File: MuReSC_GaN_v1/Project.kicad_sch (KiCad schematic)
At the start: 19 parts, among them IC1 STM32G474RET6, IC10 UCC12040DVE, IC2 TPSM5601R5HRDAR, IC3 ISO7720FQDQ1, IC4 ISO7720FQDQ1, IC5 ISO7720FQDQ1, IC6 ISO7720FQDQ1, IC7 UCC12040DVE, IC8 UCC12040DVE, IC9 UCC12040DVE, J1 62000211121, J2 62000211121, J3 691214110002, J4 691214110002, J5 691214110002, J6 691214110002

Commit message: finito schema
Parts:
- removed J1: 62000211121, 62000211121, symbol SamacSys_Parts:62000211121
- removed J3, J4, J5, J6: 691214110002, 691214110002, symbol SamacSys_Parts:691214110002
- added BEAD1, BEAD2: BLM15AG601SZ1D, NFZ15SG152SN10B, symbol SamacSys_Parts:BLM15AG601SZ1D
- added C1: C1812C124J1GACTU, C1812, symbol SamacSys_Parts:C1812C124J1GACTU
- added C2: C1206C821J1GACTU, C1206, symbol SamacSys_Parts:C1206C821J1GACTU
- added C3: C1812C105K1RACTU, C1812, symbol SamacSys_Parts:C1812C105K1RACTU
- added CCV1, CCV2: C1210C107M8PACTU, C1210, symbol SamacSys_Parts:C1210C107M8PACTU
- added CD1, CD2, CD3, CD4, CISOP1, CISOP2, CISOP3, CISOP4, CISOS1, CISOS2, CISOS3, CISOS4, CLD2, CM5, CM8: GRT155R70J105KE01D, CAPC1005X55N, symbol SamacSys_Parts:GRT155R70J105KE01D
- added CFT1, CFT2, CFT3, CFT4: NFM15PC104R1A3D, NFM15CC222D1A3D, symbol SamacSys_Parts:NFM15PC104R1A3D
- added CIN1, CIN2: GRJ31CZ72A475KE01L, CAPC3216X190N, symbol SamacSys_Parts:GRJ31CZ72A475KE01L
- added CLD1: GRM155Z71A105KE01J, CAPC1005X55N, symbol SamacSys_Parts:GRM155Z71A105KE01J
- added CM0: GRM155R61A475MEAAD, CAPC1005X55N, symbol SamacSys_Parts:GRM155R61A475MEAAD
- added CM1, CM10, CM2, CM3, CM4, CM6, CM7, CM9, CTP1, CTP2, CTP3, CTP4, CTS1, CTS2, CTS3, CTS4: C0402C104K8RAC7867, CAPC1005X55N, symbol SamacSys_Parts:C0402C104K8RAC7867
- added COH1, COH2: GJM0335C1E6R8DB01D, CAPC0603X33N, symbol SamacSys_Parts:GJM0335C1E6R8DB01D
- added COL1, COL2: C, Capacitor_SMD:C_0201_0603Metric_Pad0.64x0.40mm_HandSolder, symbol Device:C
- added CTPB1, CTPB2, CTPB3, CTPB4, CTSB1, CTSB2, CTSB3, CTSB4: C0603C106M8PAC7411, C0603, symbol SamacSys_Parts:C0603C106M8PAC7411
- added D1, D2: ESDALC6V1-1U2, ESDALC6V11U2, symbol SamacSys_Parts:ESDALC6V1-1U2
- added IC11, IC12, IC13, IC14: LMG1020YFFR, BGA6C40P2X3_86X126X62, symbol SamacSys_Parts:LMG1020YFFR
- added J1: 62000211121_x6, SamacSys_Parts:62000211121_x6, symbol SamacSys_Parts:62000211121_x6
- added J3, J4: 62000211121_x1, SamacSys_Parts:62000211121_x1, symbol SamacSys_Parts:62000211121_x1
- added L1: L, Inductor_SMD:L_0603_1608Metric, symbol Device:L
- added P1, P2: 691214110002, 691214110002, symbol SamacSys_Parts:691214110002
- added Q1, Q2, Q3, Q4: GS61004B-TR, GS61004BTR, symbol SamacSys_Parts:GS61004B-TR
- added RF1, RM1: MCS04020D1002BE000, RESC1005X37N, symbol SamacSys_Parts:MCS04020D1002BE000
- added RF2: MCS04020D2491BE000, RESC1005X37N, symbol SamacSys_Parts:MCS04020D2491BE000
- added RH1, RH2, RH3, RH4, RL1, RL2, RL3, RL4: MCS0402MC1008FE000, RESC1005X37N, symbol SamacSys_Parts:MCS0402MC1008FE000
- added RS1, RS2, RS3, RS4, RS5, RS6, RS7, RS8: R, Resistor_SMD:R_0603_1608Metric_Pad0.98x0.95mm_HandSolder, symbol Device:R
- added RUB1: MCS04020C3300FE000, RESC1005X37N, symbol SamacSys_Parts:MCS04020C3300FE000
- added RUB2: MCS04020C1003FE000, RESC1005X37N, symbol SamacSys_Parts:MCS04020C1003FE000
- added S1, S2: PTS526_SK15_SMTR2_LFS, PTS526SK15SMTR2LFS, symbol SamacSys_Parts:PTS526_SK15_SMTR2_LFS
- added Y1: NX3215SA-32.768K-STD-MUS-2, NX3215SA32768KSTDMUS2, symbol SamacSys_Parts:NX3215SA-32.768K-STD-MUS-2
- added Y2: NX3225SA-24.000MHZ-STD-CSR-1, NX3225SA24000MHZSTDCSR1, symbol SamacSys_Parts:NX3225SA-24.000MHZ-STD-CSR-1
- added Z3, Z4: TSZU52C3V3_RGG, TSZU52C3V3RGG, symbol SamacSys_Parts:TSZU52C3V3_RGG
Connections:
- net VDD3V3: now reaches IC6.1 (VCC1)
- net VDD3V3: now also IC1.1 (VBAT), IC1.16 (VDD_1), IC1.32 (VDD_2), IC1.48 (VDD_3), IC1.64 (VDD_4), IC3.1 (VCC1), IC4.1 (VCC1), IC5.1 (VCC1), PS1.4 (VOUT), BEAD2.1, CISOP1.1, CISOP2.1, CISOP3.1, CISOP4.1, CLD2.1, CM0.2, CM2.1, CM3.1, CM4.1, CM5.1, CM6.2, J1.1, S2.1 (COM_1), S2.2 (COM_2)
- net HRTIM1_CHD1: now reaches IC6.2 (INA)
- net HRTIM1_CHD1: now also IC1.36 (PB14)
- net HRTIM1_CHD2: now reaches IC6.3 (INB)
- net HRTIM1_CHD2: now also IC1.37 (PB15)
- net GND: now reaches IC6.4 (GND1)
- net GND: now also IC1.15 (VSS_1), IC1.27 (VSSA), IC1.31 (VSS_2), IC1.47 (VSS_3), IC1.63 (VSS_4), IC10.10 (NC_4), IC10.11 (NC_5), IC10.12 (NC_6), IC10.15 (GNDS_2), IC10.16 (GNDS_3), IC10.2 (GNDP), IC10.4 (SYNC), IC10.6 (NC_1), IC10.7 (NC_2), IC10.8 (NC_3), IC10.9 (GNDS_1), IC2.10 (AGND), IC2.12 (PGOOD), IC3.4 (GND1), IC4.4 (GND1), IC5.4 (GND1), IC6.5 (GND2), IC7.2 (GNDP), IC7.4 (SYNC), IC7.6 (NC_1), IC7.7 (NC_2), IC7.8 (NC_3), IC8.2 (GNDP), IC8.4 (SYNC), IC8.6 (NC_1), IC8.7 (NC_2), IC8.8 (NC_3), IC9.2 (GNDP), IC9.4 (SYNC), IC9.6 (NC_1), IC9.7 (NC_2), IC9.8 (NC_3), PS1.2 (GND), PS1.7 (PAD), Z1.2 (A), Z2.2 (A), C3.2, CCV1.2, CCV2.2, CD4.2, CFT4.2 (GND_1), CFT4.4 (GND_2), CIN1.2, CIN2.2, CISOP1.2, CISOP2.2, CISOP3.2, CISOP4.2, CISOS4.2, CLD1.2, CLD2.2, CM0.1, CM1.2, CM10.2, CM2.2, CM3.2, CM4.2, CM5.2, CM6.1, CM7.1, CM8.2, CM9.2, COH1.1, COH2.1, COL1.1, COL2.1, CTP1.2, CTP2.2, CTP3.2, CTP4.2, CTPB1.2, CTPB2.2, CTPB3.2, CTPB4.2, CTS4.2, CTSB4.2, D1.2 (A), D2.2 (A), IC14.B1 (GND), J1.3, P1.2, P2.2, Q4.3 (S), RF2.1, RM1.2, RS2.2, RS3.2, RS6.2, RS7.2, RUB2.2, S1.3 (NO_1), S1.4 (NO_2), Y2.2 (GND_1), Y2.4 (GND_2), Z3.2 (A), Z4.2 (A)
- net INN4: now reaches IC6.6 (OUTB)
- net INN4: now also IC14.C2 (IN-)
- net INP4: now reaches IC6.7 (OUTA)
- net INP4: now also IC14.C1 (IN+)
- net VDDI4: now reaches IC6.8 (VCC2)
- net VDDI4: now also IC10.13 (SEL), IC10.14 (VISO), CD4.1, CFT4.1 (IN), CISOS4.1, CTS4.1, CTSB4.1
- net VDD5V: now reaches PS1.1 (EN)
- net VDD5V: now also IC10.1 (EN), IC10.3 (VINP), IC2.7 (VOUT_1), IC2.8 (VOUT_2), IC7.1 (EN), IC7.3 (VINP), IC8.1 (EN), IC8.3 (VINP), IC9.1 (EN), IC9.3 (VINP), PS1.6 (VIN), CCV1.1, CCV2.1, CLD1.1, CTP1.1, CTP2.1, CTP3.1, CTP4.1, CTPB1.1, CTPB2.1, CTPB3.1, CTPB4.1, RF1.1
- net COMP1_INP: now reaches Z2.1 (K)
- net COMP1_INP: now also IC1.25 (PB1), RS3.1, RS4.2
- net ADC1_IN1: now reaches IC1.12 (PA0)
- net ADC1_IN1: now also Z1.1 (K), RS1.2, RS2.1
- net ADC2_IN2: now reaches IC1.13 (PA1)
- net ADC2_IN2: now also RS7.1, RS8.2, Z3.1 (K)
- net STLINK_RX: now reaches IC1.14 (PA2)
- net STLINK_RX: now also J2.2
- net STLINK_TX: now reaches IC1.17 (PA3)
- net STLINK_TX: now also J2.1
- net COMP1_INM: now reaches IC1.18 (PA4)
- net COMP1_INM: now also J3.1
- net COMP2_INM: now reaches IC1.19 (PA5)
- net COMP2_INM: now also J4.1
- net UBUTT: now reaches IC1.2 (PC13)
- net UBUTT: now also D2.1 (K), RUB1.2, S2.3 (NO_1), S2.4 (NO_2)
- net COMP2_INP: now reaches IC1.21 (PA7)
- net COMP2_INP: now also RS5.2, RS6.1, Z4.1 (K)
- net VREFP: now reaches IC1.28 (VREF+)
- net VREFP: now also BEAD2.2, CM7.2, CM8.1
- net at IC1.29 (VDDA): now also BEAD1.2
- net OSC32_IN: now reaches IC1.3 (PC14-OSC32_IN)
- net OSC32_IN: now also COL1.2, Y1.1
- net HRTIM1_CHC1: now reaches IC1.34 (PB12)
- net HRTIM1_CHC1: now also IC5.2 (INA)
- net HRTIM1_CHC2: now reaches IC1.35 (PB13)
- net HRTIM1_CHC2: now also IC5.3 (INB)
- net OSC32_OUT: now reaches IC1.4 (PC15-OSC32_OUT)
- net OSC32_OUT: now also COL2.2, Y1.2
- net HRTIM1_CHA1: now reaches IC1.42 (PA8)
- net HRTIM1_CHA1: now also IC3.2 (INA)
- net HRTIM1_CHA2: now reaches IC1.43 (PA9)
- net HRTIM1_CHA2: now also IC3.3 (INB)
- net HRTIM1_CHB1: now reaches IC1.44 (PA10)
- net HRTIM1_CHB1: now also IC4.2 (INA)
- net HRTIM1_CHB2: now reaches IC1.45 (PA11)
- net HRTIM1_CHB2: now also IC4.3 (INB)
- net T_SWDIO: now reaches IC1.49 (PA13)
- net T_SWDIO: now also J1.4
- net OSC24_IN: now reaches IC1.5 (PF0-OSC_IN)
- net OSC24_IN: now also COH2.2, Y2.1 (CRYSTAL_1)
- net T_SWCLK: now reaches IC1.50 (PA14)
- net T_SWCLK: now also J1.2
- net OSC24_OUT: now reaches IC1.6 (PF1-OSC_OUT)
- net OSC24_OUT: now also COH1.2, Y2.3 (CRYSTAL_2)
- net at IC1.61 (PB8-BOOT0): now also RM1.1
- net NRST: now reaches IC1.7 (PG10-NRST)
- net NRST: now also CM9.1, D1.1 (K), J1.5, S1.1 (COM_1), S1.2 (COM_2)
- net S2: now reaches IC8.10 (NC_4)
- net S2: now also IC4.5 (GND2), IC8.11 (NC_5), IC8.12 (NC_6), IC8.15 (GNDS_2), IC8.16 (GNDS_3), IC8.9 (GNDS_1), C3.1, CD2.2, CFT2.2 (GND_1), CFT2.4 (GND_2), CISOS2.2, CTS2.2, CTSB2.2, IC12.B1 (GND), P2.1, Q2.3 (S), Q3.1 (D), RS1.1, RS4.1
- net VDDI2: now reaches IC8.13 (SEL)
- net VDDI2: now also IC4.8 (VCC2), IC8.14 (VISO), CD2.1, CFT2.1 (IN), CISOS2.1, CTS2.1, CTSB2.1
- net S1: now reaches IC7.10 (NC_4)
- net S1: now also IC3.5 (GND2), IC7.11 (NC_5), IC7.12 (NC_6), IC7.15 (GNDS_2), IC7.16 (GNDS_3), IC7.9 (GNDS_1), C1.1, CD1.2, CFT1.2 (GND_1), CFT1.4 (GND_2), CISOS1.2, CTS1.2, CTSB1.2, IC11.B1 (GND), Q1.3 (S), Q2.1 (D)
- net VDDI1: now reaches IC7.13 (SEL)
- net VDDI1: now also IC3.8 (VCC2), IC7.14 (VISO), CD1.1, CFT1.1 (IN), CISOS1.1, CTS1.1, CTSB1.1
- net S3: now reaches IC5.5 (GND2)
- net S3: now also IC9.10 (NC_4), IC9.11 (NC_5), IC9.12 (NC_6), IC9.15 (GNDS_2), IC9.16 (GNDS_3), IC9.9 (GNDS_1), C2.2, CD3.2, CFT3.2 (GND_1), CFT3.4 (GND_2), CISOS3.2, CTS3.2, CTSB3.2, IC13.B1 (GND), L1.2, Q3.3 (S), Q4.1 (D)
- net INN3: now reaches IC5.6 (OUTB)
- net INN3: now also IC13.C2 (IN-)
- net INP3: now reaches IC5.7 (OUTA)
- net INP3: now also IC13.C1 (IN+)
- net VDDI3: now reaches IC5.8 (VCC2)
- net VDDI3: now also IC9.13 (SEL), IC9.14 (VISO), CD3.1, CFT3.1 (IN), CISOS3.1, CTS3.1, CTSB3.1
- net INN1: now reaches IC3.6 (OUTB)
- net INN1: now also IC11.C2 (IN-)
- net INP1: now reaches IC3.7 (OUTA)
- net INP1: now also IC11.C1 (IN+)
- net INN2: now reaches IC4.6 (OUTB)
- net INN2: now also IC12.C2 (IN-)
- net INP2: now reaches IC4.7 (OUTA)
- net INP2: now also IC12.C1 (IN+)
- net VDD48V: now reaches IC2.1 (VIN_1)
- net VDD48V: now also IC2.14 (VIN_2), IC2.2 (EN), CIN1.1, CIN2.1, P1.1, Q1.1 (D), RS5.1, RS8.1
- net TPSFB: now reaches IC2.9 (FB)
- net TPSFB: now also RF1.2, RF2.2
- new net: CFT2.3 (OUT), IC12.A1 (VDD)
- new net: C1.2, C2.1, L1.1
- new net: Q2.2 (G), RH2.2, RL2.2
- new net: CM10.1, RUB1.1, RUB2.1
- new net: BEAD1.1, CM1.1
- new net: Q3.2 (G), RH3.2, RL3.2
- new net: CFT4.3 (OUT), IC14.A1 (VDD)
- new net: Q1.2 (G), RH1.2, RL1.2
- new net: CFT1.3 (OUT), IC11.A1 (VDD)
- new net: Q4.2 (G), RH4.2, RL4.2
- new net: CFT3.3 (OUT), IC13.A1 (VDD)
- new net IG1RH: IC11.A2 (OUTH), RH1.1
- new net IG1RL: IC11.B2 (OUTL), RL1.1
- new net IG2RH: IC12.A2 (OUTH), RH2.1
- new net IG2RL: IC12.B2 (OUTL), RL2.1
- new net IG3RH: IC13.A2 (OUTH), RH3.1
- new net IG3RL: IC13.B2 (OUTL), RL3.1
- new net IG4RH: IC14.A2 (OUTH), RH4.1
- new net IG4RL: IC14.B2 (OUTL), RL4.1
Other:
- note added: "BOTTONI"
- note added: "CAPACITA FILRO QUI?"
- note added: "Connettori"
- note added: "DCDC 48V to 5V"
- note added: "LDO"
- note added: "MICRO"
- note added: "OSCILLATORI"
- note added: "SENSING"
- moved on the sheet: IC1, IC2, IC3, IC7, PS1, Z1, Z2

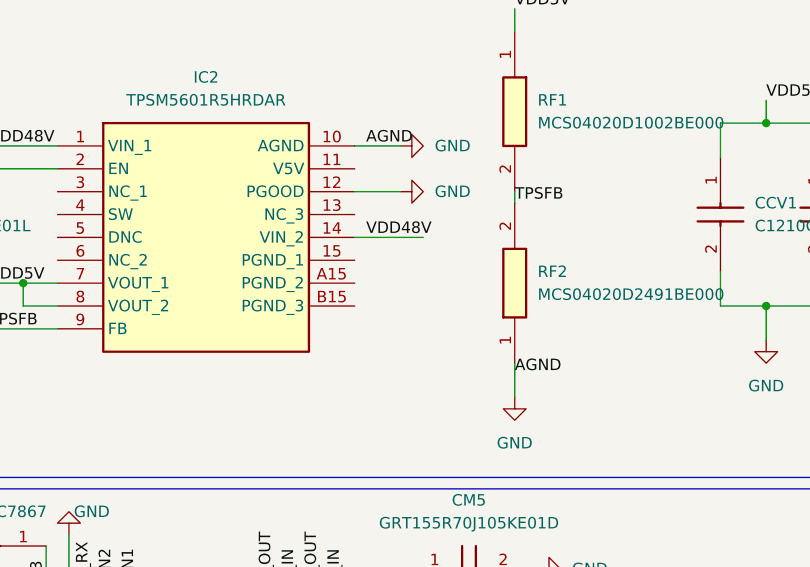
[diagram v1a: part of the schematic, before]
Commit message: schematic finished + start layout
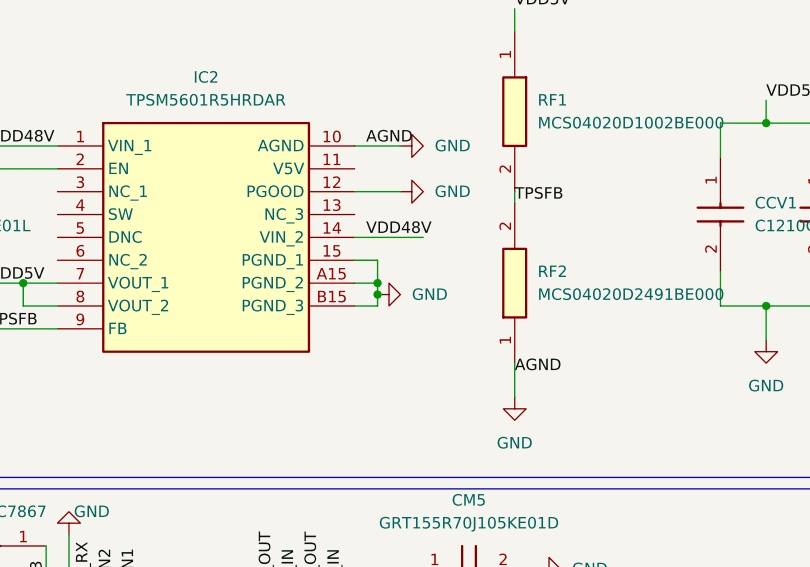
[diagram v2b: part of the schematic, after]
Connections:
- net GND: now also IC2.15 (PGND_1), IC2.A15 (PGND_2), IC2.B15 (PGND_3)
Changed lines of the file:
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@@
   (junction (at 328.93 179.07) (diameter 0) (color 0 0 0 0)
   )
+  (junction (at 92.71 46.99) (diameter 0) (color 0 0 0 0)
+  )
   (junction (at 326.39 255.27) (diameter 0) (color 0 0 0 0)
   )
@@
   (junction (at 91.44 168.91) (diameter 0) (color 0 0 0 0)
   )
+  (junction (at 92.71 45.72) (diameter 0) (color 0 0 0 0)
+  )
   (junction (at 326.39 341.63) (diameter 0) (color 0 0 0 0)
   )
@@
     (stroke (width 0) (type default))
   )
+  (wire (pts (xy 92.71 43.18) (xy 92.71 45.72))
+    (stroke (width 0) (type default))
+  )
   (wire (pts (xy 130.81 44.45) (xy 130.81 48.26))
     (stroke (width 0) (type default))
@@
     (stroke (width 0) (type default))
   )
+  (wire (pts (xy 90.17 45.72) (xy 92.71 45.72))
+    (stroke (width 0) (type default))
+  )
   (wire (pts (xy 467.36 320.04) (xy 472.44 320.04))
     (stroke (width 0) (type default))
@@
     (stroke (width 0) (type default))
   )
+  (wire (pts (xy 92.71 46.99) (xy 92.71 48.26))
+    (stroke (width 0) (type default))
+  )
   (wire (pts (xy 228.6 25.4) (xy 236.22 25.4))
     (stroke (width 0) (type default))
@@
     (stroke (width 0) (type default))
   )
+  (wire (pts (xy 90.17 48.26) (xy 92.71 48.26))
+    (stroke (width 0) (type default))
+  )
   (wire (pts (xy 320.04 232.41) (xy 320.04 229.87))
     (stroke (width 0) (type default))
@@
     (stroke (width 0) (type default))
   )
+  (wire (pts (xy 90.17 43.18) (xy 92.71 43.18))
+    (stroke (width 0) (type default))
+  )
   (wire (pts (xy 19.05 49.53) (xy 24.13 49.53))
     (stroke (width 0) (type default))
@@
     (stroke (width 0) (type default))
   )
+  (wire (pts (xy 92.71 45.72) (xy 92.71 46.99))
+    (stroke (width 0) (type default))
+  )
   (wire (pts (xy 328.93 118.11) (xy 328.93 120.65))
     (stroke (width 0) (type default))
@@
         )
       )
+    )
+  )
+  (symbol (lib_id "power:GND") (at 92.71 46.99 90) (unit 1)
+    (in_bom yes) (on_board yes) (dnp no) (fields_autoplaced)
+    (property "Reference" "#PWR071" (at 99.06 46.99 0)
+      (effects (font (size 1.27 1.27)) hide)
+    )
+    (property "Value" "GND" (at 96.52 46.99 90)
+      (effects (font (size 1.27 1.27)) (justify right))
+    )
+    (property "Footprint" "" (at 92.71 46.99 0)
+      (effects (font (size 1.27 1.27)) hide)
+    )
+    (property "Datasheet" "" (at 92.71 46.99 0)
+      (effects (font (size 1.27 1.27)) hide)
+    )
+    (pin "1")
+    (instances
+      (project "Project"
+        (path "/370b4fcc-a080-452a-8e5f-5eff99707865"
+          (reference "#PWR071") (unit 1)
+        )
+      )

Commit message: placement
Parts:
- removed L1: L, Inductor_SMD:L_0603_1608Metric, symbol Device:L
- added L1: 2222SQ-221GEC, 2222SQ221GEC, symbol SamacSys_Parts:2222SQ-221GEC
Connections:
- net S3: now also L1.2
- net at C1.2, C2.1: now also L1.1
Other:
- moved on the sheet: C1, C2

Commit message: lauyout update
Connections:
- net HRTIM1_CHA1: now also IC4.3 (INB); no longer IC3.2 (INA)
- net HRTIM1_CHA2: now also IC4.2 (INA); no longer IC3.3 (INB)
- net HRTIM1_CHB1: now also IC3.3 (INB); no longer IC4.2 (INA)
- net HRTIM1_CHB2: now also IC3.2 (INA); no longer IC4.3 (INB)
- net HRTIM1_CHC1: now also IC6.3 (INB); no longer IC5.2 (INA)
- net HRTIM1_CHC2: now also IC6.2 (INA); no longer IC5.3 (INB)
- net HRTIM1_CHD1: now also IC5.3 (INB); no longer IC6.2 (INA)
- net HRTIM1_CHD2: now also IC5.2 (INA); no longer IC6.3 (INB)
- net G2: now reaches Q2.2 (G), RH2.2, RL2.2
- net G3: now reaches Q3.2 (G), RH3.2, RL3.2
- net G1: now reaches Q1.2 (G), RH1.2, RL1.2
- net G4: now reaches Q4.2 (G), RH4.2, RL4.2
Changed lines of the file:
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@@
+    (effects (font (size 1.27 1.27)) (justify left bottom))
+  )
+  (label "G1" (at 492.76 119.38 0) (fields_autoplaced)
     (effects (font (size 1.27 1.27)) (justify left bottom))
   )
@@
     (effects (font (size 1.27 1.27)) (justify left bottom))
   )
-  (label "HRTIM1_CHA1" (at 184.15 121.92 0) (fields_autoplaced)
+  (label "HRTIM1_CHB2" (at 184.15 121.92 0) (fields_autoplaced)
     (effects (font (size 1.27 1.27)) (justify left bottom))
   )
@@
     (effects (font (size 1.27 1.27)) (justify left bottom))
   )
-  (label "HRTIM1_CHC2" (at 182.88 246.38 0) (fields_autoplaced)
+  (label "HRTIM1_CHD1" (at 182.88 246.38 0) (fields_autoplaced)
     (effects (font (size 1.27 1.27)) (justify left bottom))
   )
@@
     (effects (font (size 1.27 1.27)) (justify left bottom))
   )
-  (label "HRTIM1_CHD1" (at 180.34 323.85 0) (fields_autoplaced)
+  (label "HRTIM1_CHC2" (at 180.34 323.85 0) (fields_autoplaced)
     (effects (font (size 1.27 1.27)) (justify left bottom))
   )
@@
     (effects (font (size 1.27 1.27)) (justify left bottom))
   )
+  (label "G4" (at 492.76 320.04 0) (fields_autoplaced)
+    (effects (font (size 1.27 1.27)) (justify left bottom))
+  )
   (label "VDD3V3" (at 241.3 21.59 0) (fields_autoplaced)
     (effects (font (size 1.27 1.27)) (justify left bottom))
   )
-  (label "HRTIM1_CHB2" (at 184.15 186.69 0) (fields_autoplaced)
+  (label "HRTIM1_CHA1" (at 184.15 186.69 0) (fields_autoplaced)
     (effects (font (size 1.27 1.27)) (justify left bottom))
   )
@@
     (effects (font (size 1.27 1.27)) (justify left bottom))
   )
+  (label "G2" (at 492.76 177.8 0) (fields_autoplaced)
+    (effects (font (size 1.27 1.27)) (justify left bottom))
+  )
   (label "INP3" (at 223.52 243.84 0) (fields_autoplaced)
     (effects (font (size 1.27 1.27)) (justify left bottom))
@@
     (effects (font (size 1.27 1.27)) (justify left bottom))
   )
-  (label "HRTIM1_CHC1" (at 182.88 243.84 0) (fields_autoplaced)
+  (label "HRTIM1_CHD2" (at 182.88 243.84 0) (fields_autoplaced)
     (effects (font (size 1.27 1.27)) (justify left bottom))
   )
@@
     (effects (font (size 1.27 1.27)) (justify left bottom))
   )
+  (label "G3" (at 492.76 242.57 0) (fields_autoplaced)
+    (effects (font (size 1.27 1.27)) (justify left bottom))
+  )
   (label "T_SWCLK" (at 274.32 46.99 0) (fields_autoplaced)
     (effects (font (size 1.27 1.27)) (justify left bottom))
@@
     (effects (font (size 1.27 1.27)) (justify left bottom))
   )
-  (label "HRTIM1_CHB1" (at 184.15 184.15 0) (fields_autoplaced)
+  (label "HRTIM1_CHA2" (at 184.15 184.15 0) (fields_autoplaced)
     (effects (font (size 1.27 1.27)) (justify left bottom))
   )
@@
     (effects (font (size 1.27 1.27)) (justify left bottom))
   )
-  (label "HRTIM1_CHA2" (at 184.15 124.46 0) (fields_autoplaced)
+  (label "HRTIM1_CHB1" (at 184.15 124.46 0) (fields_autoplaced)
     (effects (font (size 1.27 1.27)) (justify left bottom))
   )
@@
     (effects (font (size 1.27 1.27)) (justify left bottom))
   )
-  (label "HRTIM1_CHD2" (at 180.34 326.39 0) (fields_autoplaced)
-    (effects (font (size 1.27 1.27)) (justify left bottom))
-  )
+  (label "HRTIM1_CHC1" (at 180.34 326.39 0) (fields_autoplaced)
+    (effects (font (size 1.27 1.27)) (justify left bottom))
+  )
